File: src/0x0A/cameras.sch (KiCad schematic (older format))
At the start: 18 parts

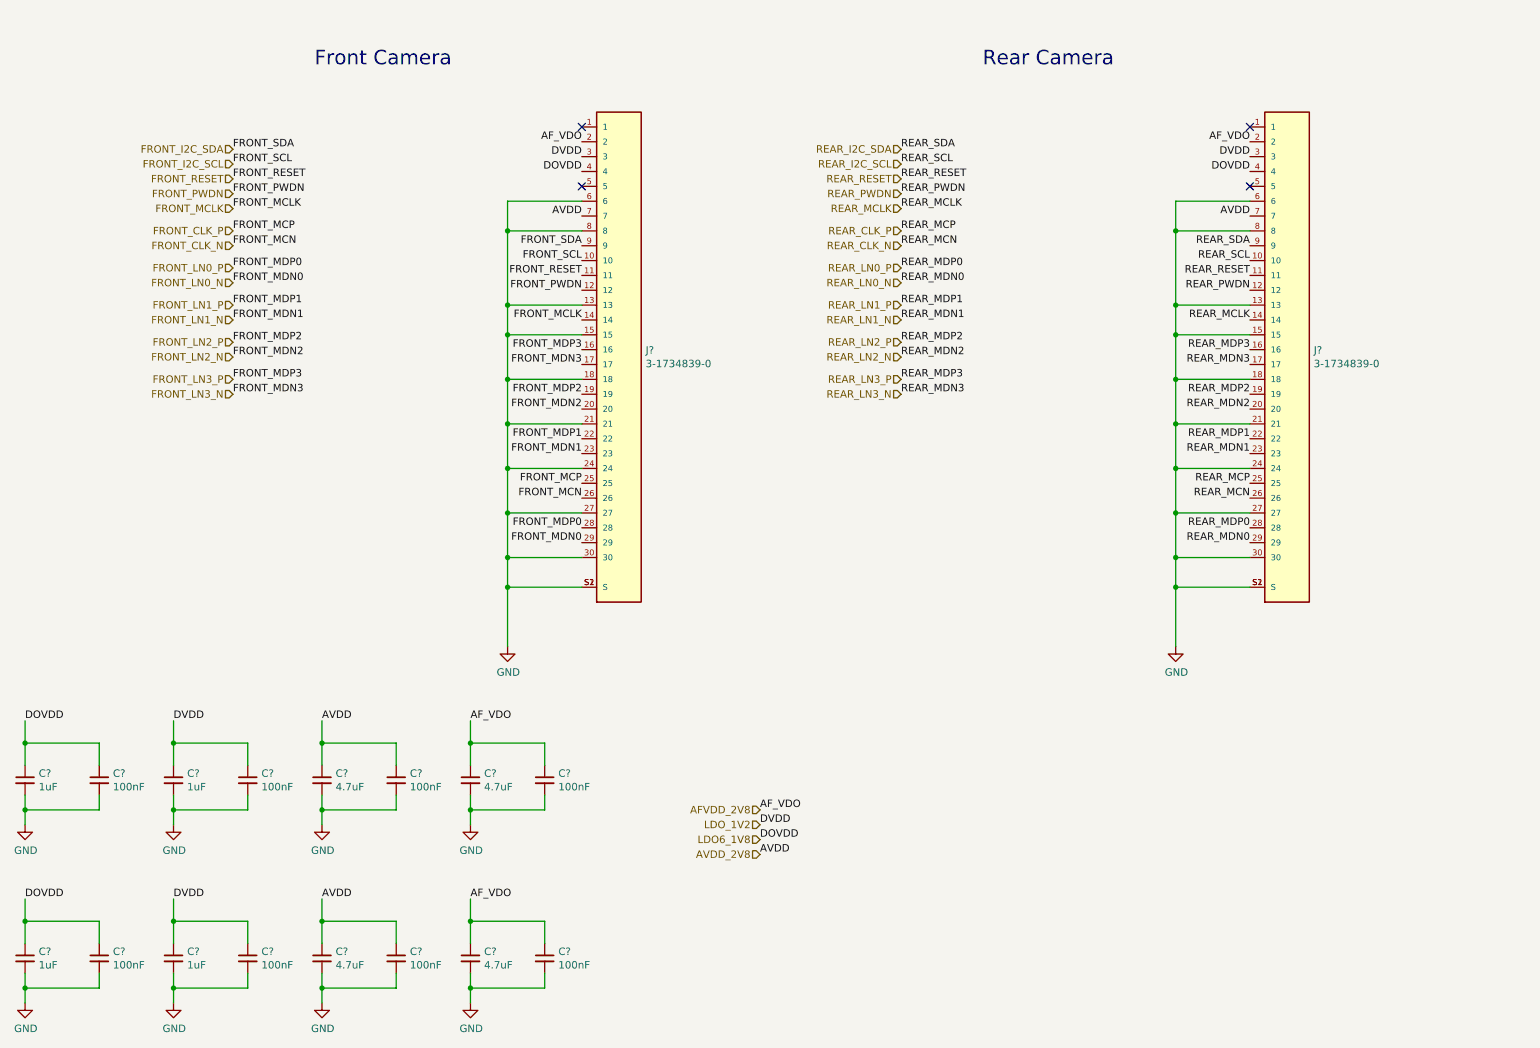
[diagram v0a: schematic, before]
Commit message: Updated schematics, started working on board layout
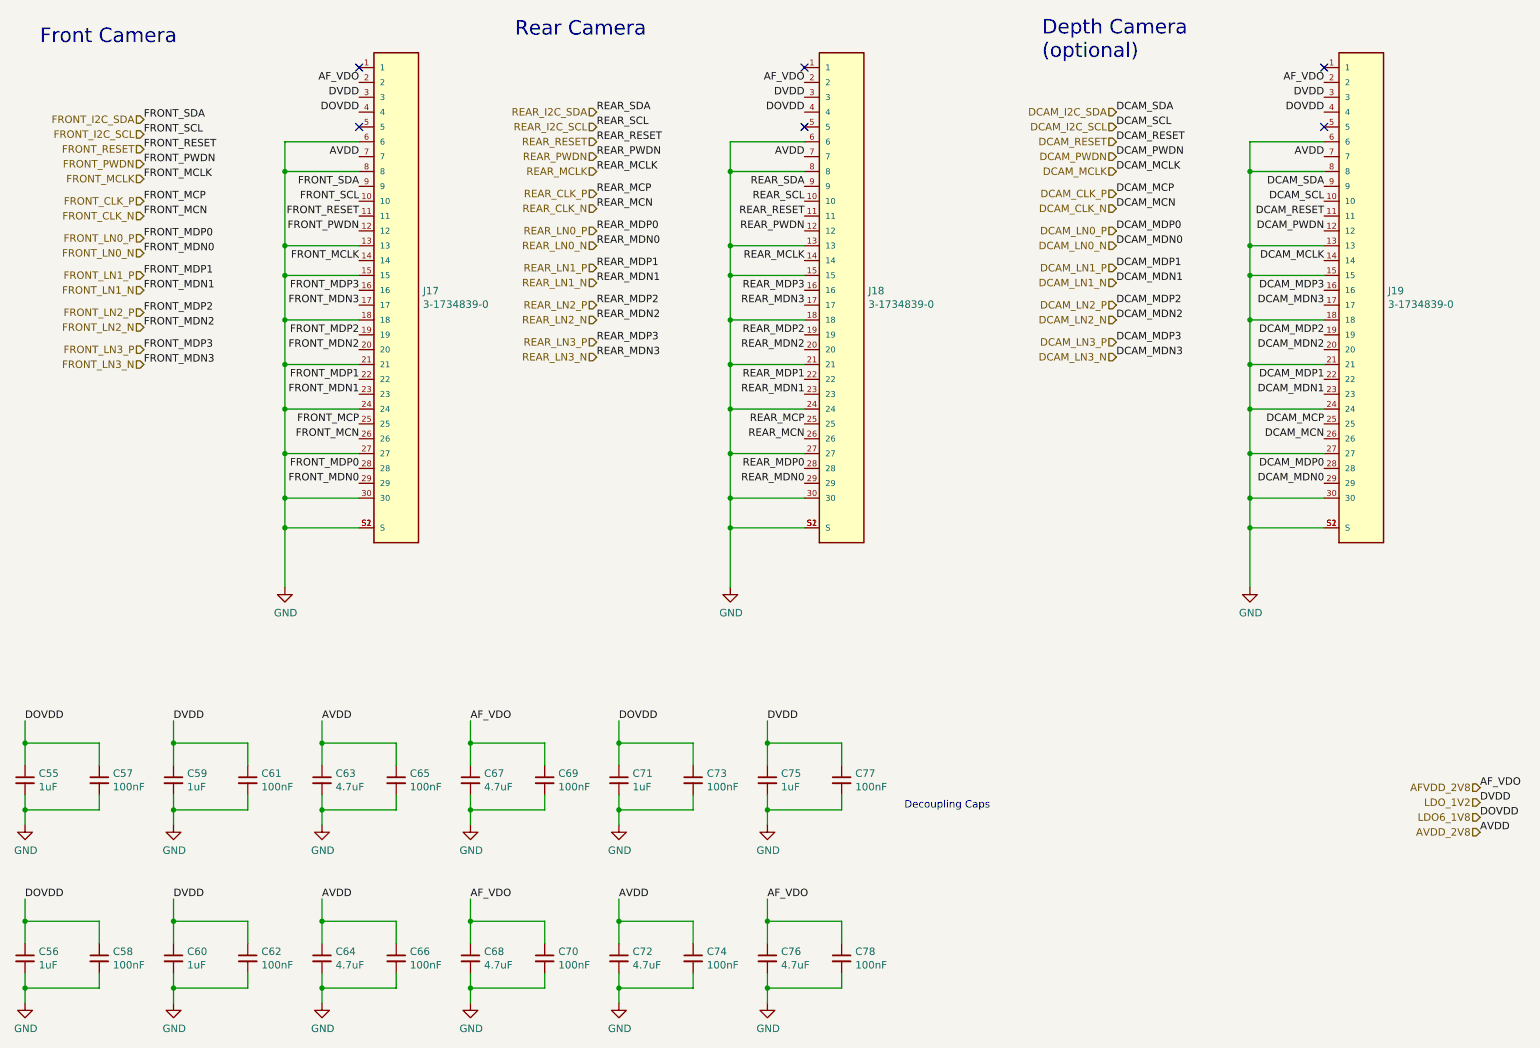
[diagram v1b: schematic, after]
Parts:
- added C71, C75: 1uF, Capacitor_SMD:C_0603_1608Metric, symbol Device:C_Small
- added C72, C76: 4.7uF, Capacitor_SMD:C_0805_2012Metric, symbol Device:C_Small
- added C73, C74, C77, C78: 100nF, Capacitor_SMD:C_0402_1005Metric, symbol Device:C_Small
- added J19: 3-1734839-0, SnapEDA Library:TE_3-1734839-0, symbol 3-1734839-0:3-1734839-0
- C55, C56, C59, C60: renamed from C?; footprint (none) -> Capacitor_SMD:C_0603_1608Metric; LCSC Part # (none) -> C15849
- C57, C58, C61, C62, C65, C66, C69, C70: renamed from C?; footprint (none) -> Capacitor_SMD:C_0402_1005Metric; LCSC Part # (none) -> C307331
- C63, C64, C67, C68: renamed from C?; footprint (none) -> Capacitor_SMD:C_0805_2012Metric; LCSC Part # (none) -> C1779
- gave numbers to parts that had none: 2
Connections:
- net AFVDD_2V8: now also C76.1, C78.1, J19.2
- net AVDD_2V8: now also C72.1, C74.1, J19.7
- net GND: now also C71.2, C72.2, C73.2, C74.2, C75.2, C76.2, C77.2, C78.2, J19.13, J19.15, J19.18, J19.21, J19.24, J19.27, J19.30, J19.6, J19.8, J19.S1 (S), J19.S2 (S)
- net LDO6_1V8: now also C71.1, C73.1, J19.4
- net LDO_1V2: now also C75.1, C77.1, J19.3
- new net DCAM_CLK_N: J19.26
- new net DCAM_CLK_P: J19.25
- new net DCAM_I2C_SCL: J19.10
- new net DCAM_I2C_SDA: J19.9
- new net DCAM_LN0_N: J19.29
- new net DCAM_LN0_P: J19.28
- new net DCAM_LN1_N: J19.23
- new net DCAM_LN1_P: J19.22
- new net DCAM_LN2_N: J19.20
- new net DCAM_LN2_P: J19.19
- new net DCAM_LN3_N: J19.17
- new net DCAM_LN3_P: J19.16
- new net DCAM_MCLK: J19.14
- new net DCAM_PWDN: J19.12
- new net DCAM_RESET: J19.11
- no-connect marks 4 -> 6
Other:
- note added: "Decoupling Caps"
- note added: "Depth Camera\n(optional)"
- moved on the sheet: J17, J18
